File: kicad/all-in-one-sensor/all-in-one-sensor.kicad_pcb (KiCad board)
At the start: 2 copper layers, 58 x 68.4 mm, 17 parts, among them J2 BH170 (0x23), J3 mmWave, J4 mmWave2, U1 EKMC1603111, U2 BME280, U3 BME680, U4 WEMOS C3/D1 Mini

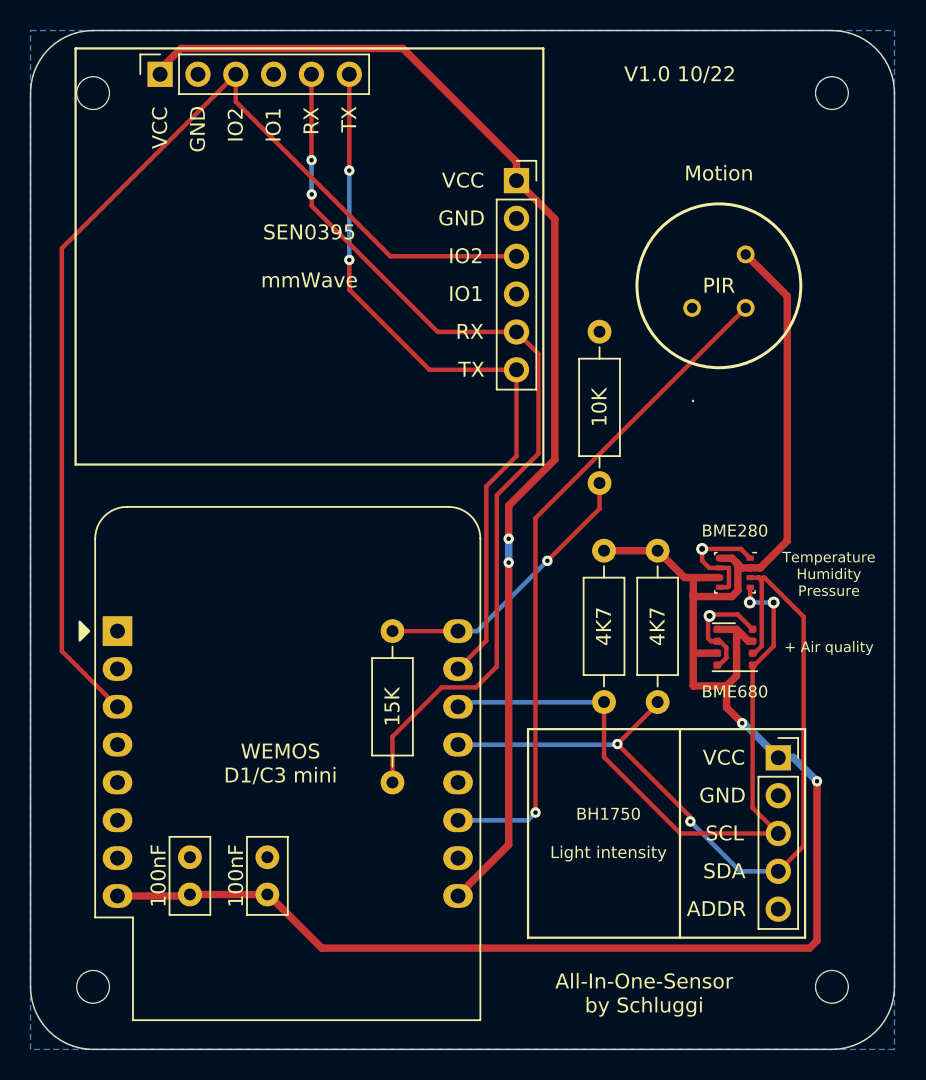
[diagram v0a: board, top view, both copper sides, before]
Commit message: closes #3: m3 mounting holes
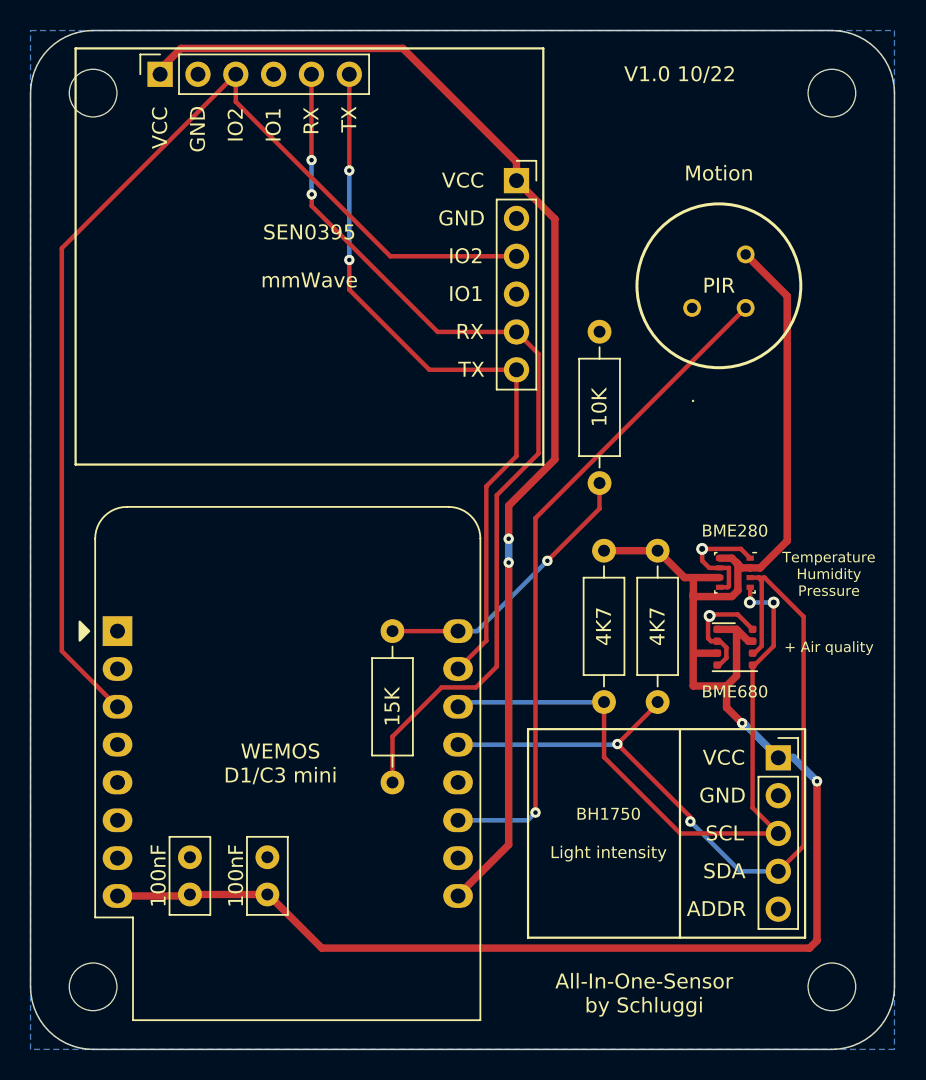
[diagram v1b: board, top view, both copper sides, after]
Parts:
- H1, H2, H3, H4: footprint MountingHole:MountingHole_2.2mm_M2 -> MountingHole:MountingHole_3.2mm_M3
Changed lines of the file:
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@@
     )
   )
-  (footprint "MountingHole:MountingHole_2.2mm_M2" (layer "F.Cu")
+  (footprint "MountingHole:MountingHole_3.2mm_M3" (layer "F.Cu")
     (at 198.2 147.2)
-    (descr "Mounting Hole 2.2mm, no annular, M2")
-    (tags "mounting hole 2.2mm no annular m2")
+    (descr "Mounting Hole 3.2mm, no annular, M3")
+    (tags "mounting hole 3.2mm no annular m3")
     (property "Sheetfile" "all-in-one-sensor.kicad_sch")
     (property "Sheetname" "")
     (attr exclude_from_pos_files)
-    (fp_text reference "H4" (at 0 -3.2) (layer "F.SilkS") hide
-      (effects (font (size 1 1) (thickness 0.15)))
-    )
-    (fp_text value "MountingHole" (at 0 3.2) (layer "F.Fab")
+    (fp_text reference "H4" (at 0 -4.2) (layer "F.SilkS") hide
+      (effects (font (size 1 1) (thickness 0.15)))
+    )
+    (fp_text value "MountingHole" (at 0 4.2) (layer "F.Fab")
       (effects (font (size 1 1) (thickness 0.15)))
     )
@@
       (effects (font (size 1 1) (thickness 0.15)))
     )
-    (fp_circle (center 0 0) (end 2.2 0) (layer "Cmts.User") (width 0.15) (fill none))
-    (fp_circle (center 0 0) (end 2.45 0) (layer "F.CrtYd") (width 0.05) (fill none))
-    (pad "" np_thru_hole circle (at 0 0) (size 2.2 2.2) (drill 2.2) (layers *.Cu *.Mask))
+    (fp_circle (center 0 0) (end 3.2 0) (layer "Cmts.User") (width 0.15) (fill none))
+    (fp_circle (center 0 0) (end 3.45 0) (layer "F.CrtYd") (width 0.05) (fill none))
+    (pad "" np_thru_hole circle (at 0 0) (size 3.2 3.2) (drill 3.2) (layers *.Cu *.Mask))
   )
   (footprint "Package_LGA:Bosch_LGA-8_2.5x2.5mm_P0.65mm_ClockwisePinNumbering" (layer "F.Cu")
@@
     )
   )
-  (footprint "MountingHole:MountingHole_2.2mm_M2" (layer "F.Cu")
+  (footprint "MountingHole:MountingHole_3.2mm_M3" (layer "F.Cu")
     (at 148.6 147.2)
-    (descr "Mounting Hole 2.2mm, no annular, M2")
-    (tags "mounting hole 2.2mm no annular m2")
+    (descr "Mounting Hole 3.2mm, no annular, M3")
+    (tags "mounting hole 3.2mm no annular m3")
     (property "Sheetfile" "all-in-one-sensor.kicad_sch")
     (property "Sheetname" "")
     (attr exclude_from_pos_files)
-    (fp_text reference "H3" (at 0 -3.2) (layer "F.SilkS") hide
-      (effects (font (size 1 1) (thickness 0.15)))
-    )
-    (fp_text value "MountingHole" (at 0 3.2) (layer "F.Fab")
+    (fp_text reference "H3" (at 0 -4.2) (layer "F.SilkS") hide
+      (effects (font (size 1 1) (thickness 0.15)))
+    )
+    (fp_text value "MountingHole" (at 0 4.2) (layer "F.Fab")
       (effects (font (size 1 1) (thickness 0.15)))
     )
@@
       (effects (font (size 1 1) (thickness 0.15)))
     )
-    (fp_circle (center 0 0) (end 2.2 0) (layer "Cmts.User") (width 0.15) (fill none))
-    (fp_circle (center 0 0) (end 2.45 0) (layer "F.CrtYd") (width 0.05) (fill none))
-    (pad "" np_thru_hole circle (at 0 0) (size 2.2 2.2) (drill 2.2) (layers *.Cu *.Mask))
+    (fp_circle (center 0 0) (end 3.2 0) (layer "Cmts.User") (width 0.15) (fill none))
+    (fp_circle (center 0 0) (end 3.45 0) (layer "F.CrtYd") (width 0.05) (fill none))
+    (pad "" np_thru_hole circle (at 0 0) (size 3.2 3.2) (drill 3.2) (layers *.Cu *.Mask))
   )
   (footprint "Resistor_THT:R_Axial_DIN0207_L6.3mm_D2.5mm_P10.16mm_Horizontal" (layer "F.Cu")
@@
     )
   )
-  (footprint "MountingHole:MountingHole_2.2mm_M2" (layer "F.Cu")
+  (footprint "MountingHole:MountingHole_3.2mm_M3" (layer "F.Cu")
     (at 198.2 87.2)
-    (descr "Mounting Hole 2.2mm, no annular, M2")
-    (tags "mounting hole 2.2mm no annular m2")
+    (descr "Mounting Hole 3.2mm, no annular, M3")
+    (tags "mounting hole 3.2mm no annular m3")
     (property "Sheetfile" "all-in-one-sensor.kicad_sch")
     (property "Sheetname" "")
     (attr exclude_from_pos_files)
-    (fp_text reference "H1" (at 0 -3.2) (layer "F.SilkS") hide
-      (effects (font (size 1 1) (thickness 0.15)))
-    )
-    (fp_text value "MountingHole" (at 0 3.2) (layer "F.Fab")
+    (fp_text reference "H1" (at 0 -4.2) (layer "F.SilkS") hide
+      (effects (font (size 1 1) (thickness 0.15)))
+    )
+    (fp_text value "MountingHole" (at 0 4.2) (layer "F.Fab")
       (effects (font (size 1 1) (thickness 0.15)))
     )
@@
       (effects (font (size 1 1) (thickness 0.15)))
     )
-    (fp_circle (center 0 0) (end 2.2 0) (layer "Cmts.User") (width 0.15) (fill none))
-    (fp_circle (center 0 0) (end 2.45 0) (layer "F.CrtYd") (width 0.05) (fill none))
-    (pad "" np_thru_hole circle (at 0 0) (size 2.2 2.2) (drill 2.2) (layers *.Cu *.Mask))
+    (fp_circle (center 0 0) (end 3.2 0) (layer "Cmts.User") (width 0.15) (fill none))
+    (fp_circle (center 0 0) (end 3.45 0) (layer "F.CrtYd") (width 0.05) (fill none))
+    (pad "" np_thru_hole circle (at 0 0) (size 3.2 3.2) (drill 3.2) (layers *.Cu *.Mask))
   )
   (footprint "Capacitor_THT:C_Disc_D5.0mm_W2.5mm_P2.50mm" (layer "F.Cu")
@@
     )
   )
-  (footprint "MountingHole:MountingHole_2.2mm_M2" (layer "F.Cu")
+  (footprint "MountingHole:MountingHole_3.2mm_M3" (layer "F.Cu")
     (at 148.6 87.2)
-    (descr "Mounting Hole 2.2mm, no annular, M2")
-    (tags "mounting hole 2.2mm no annular m2")
+    (descr "Mounting Hole 3.2mm, no annular, M3")
+    (tags "mounting hole 3.2mm no annular m3")
     (property "Sheetfile" "all-in-one-sensor.kicad_sch")
     (property "Sheetname" "")
     (attr exclude_from_pos_files)
-    (fp_text reference "H2" (at 0 -3.2) (layer "F.SilkS") hide
-      (effects (font (size 1 1) (thickness 0.15)))
-    )
-    (fp_text value "MountingHole" (at 0 3.2) (layer "F.Fab")
+    (fp_text reference "H2" (at 0 -4.2) (layer "F.SilkS") hide
+      (effects (font (size 1 1) (thickness 0.15)))
+    )
+    (fp_text value "MountingHole" (at 0 4.2) (layer "F.Fab")
       (effects (font (size 1 1) (thickness 0.15)))
     )
@@
       (effects (font (size 1 1) (thickness 0.15)))
     )
-    (fp_circle (center 0 0) (end 2.2 0) (layer "Cmts.User") (width 0.15) (fill none))
-    (fp_circle (center 0 0) (end 2.45 0) (layer "F.CrtYd") (width 0.05) (fill none))
-    (pad "" np_thru_hole circle locked (at 0 0) (size 2.2 2.2) (drill 2.2) (layers *.Cu *.Mask))
+    (fp_circle (center 0 0) (end 3.2 0) (layer "Cmts.User") (width 0.15) (fill none))
+    (fp_circle (center 0 0) (end 3.45 0) (layer "F.CrtYd") (width 0.05) (fill none))
+    (pad "" np_thru_hole circle (at 0 0) (size 3.2 3.2) (drill 3.2) (layers *.Cu *.Mask))
   )
   (gr_line (start 188 143.9) (end 188 129.9) (layer "F.SilkS") (width 0.15))
